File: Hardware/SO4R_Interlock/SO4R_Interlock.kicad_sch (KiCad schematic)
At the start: 143 parts, among them J1 USB-C 2.0 16P, J2 USB-C 2.0 16P, J3 USB-C 2.0 16P, J4 USB-C 2.0 16P, J5 Header 1x3, J6 RJ45_LED_Shielded, J7 8P8C_LED_Shielded_x4, Q1 2N7002, Q2 2N7002, Q3 2N7002, Q4 2N7002, Q5 2N7002, Q6 2N7002, Q7 2N7002, Q8 2N7002, U1 FT230XS, U10 TPD4E02B04DQA, U11 TPD4E02B04DQA, U12 TPD4E02B04DQA, U2 FT230XS, U3 FT230XS, U4 FT230XS, U5 74LVC1G07, U6 74LVC1G07, U7 74LVC1G07, U8 AVR32DB48x-xPT, U9 TPD4E02B04DQA

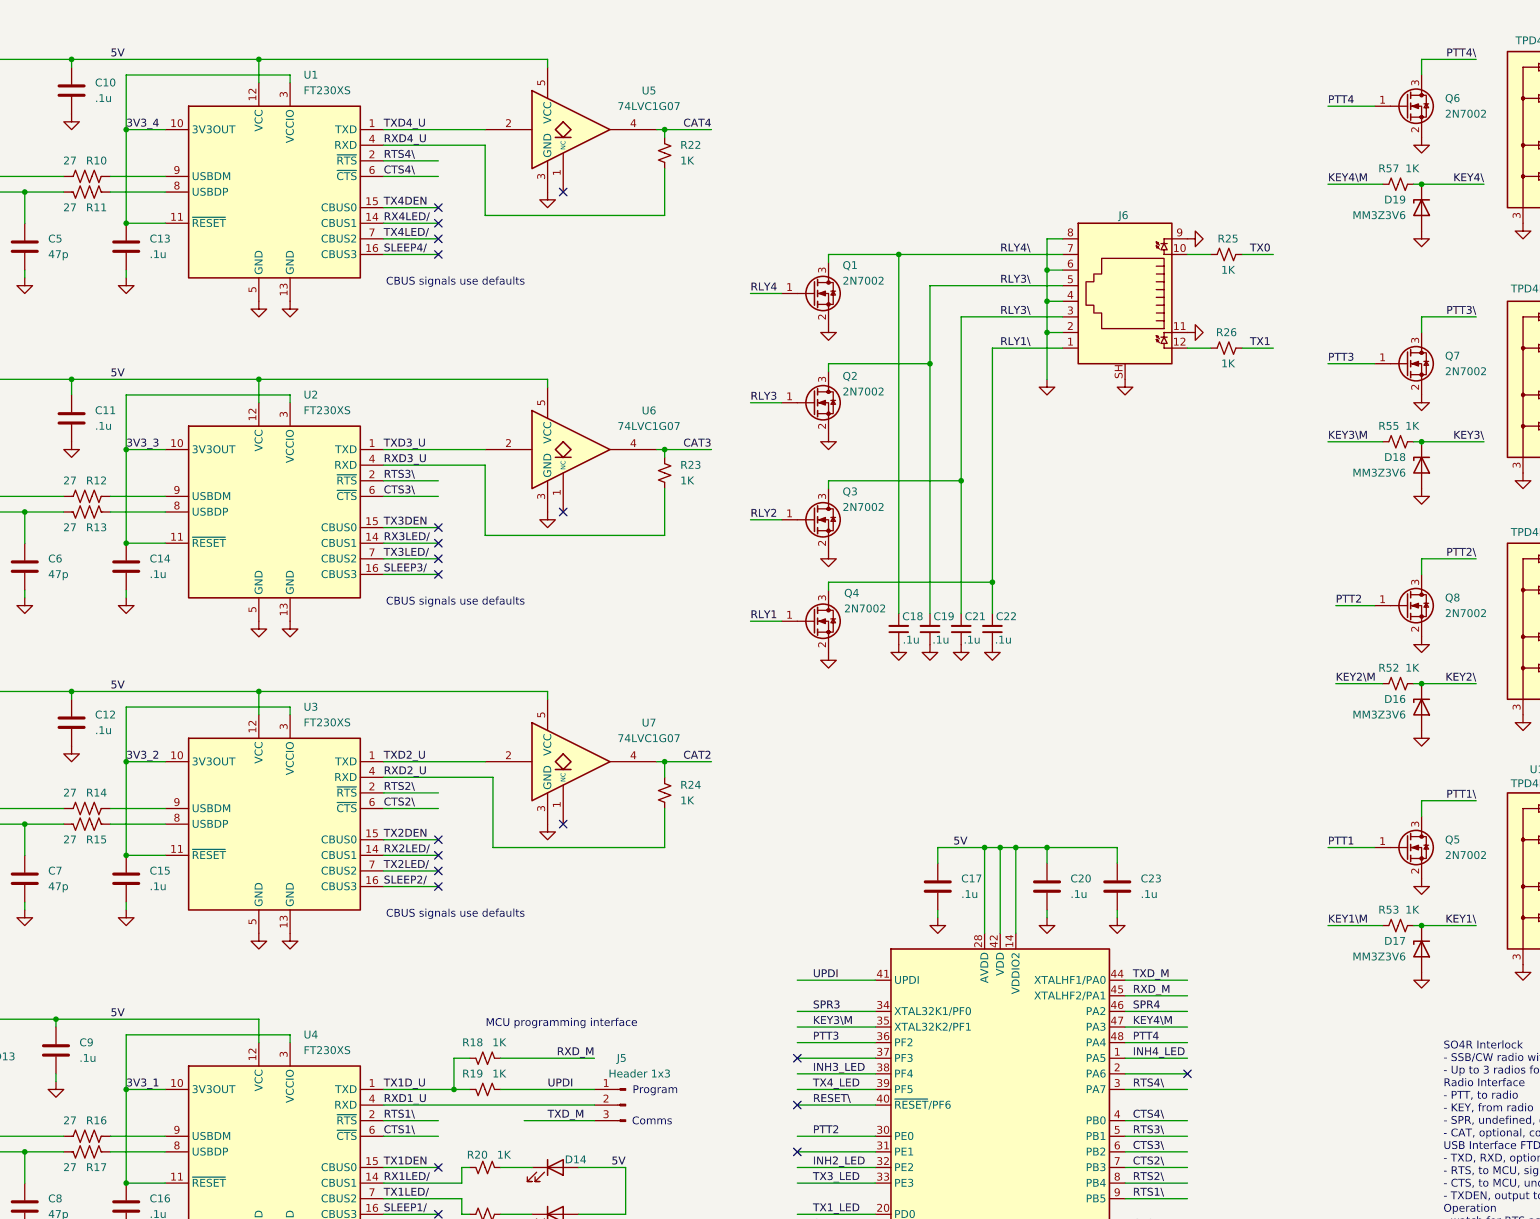
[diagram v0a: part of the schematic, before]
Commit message: Hardware   better names for PDF in documentation area   started on V2 of hardware   Connected reset\ to VDD on MCU   added .lck to .gitignore Software improves   reading RTS and KEY inputs all at one   writing KEY and PTT output as fast as possible   cleaner concept     Priority derived from RTS and KEY inputs     PTT signals derived from RTS and priority
    Relay signals derived from KEY and priority
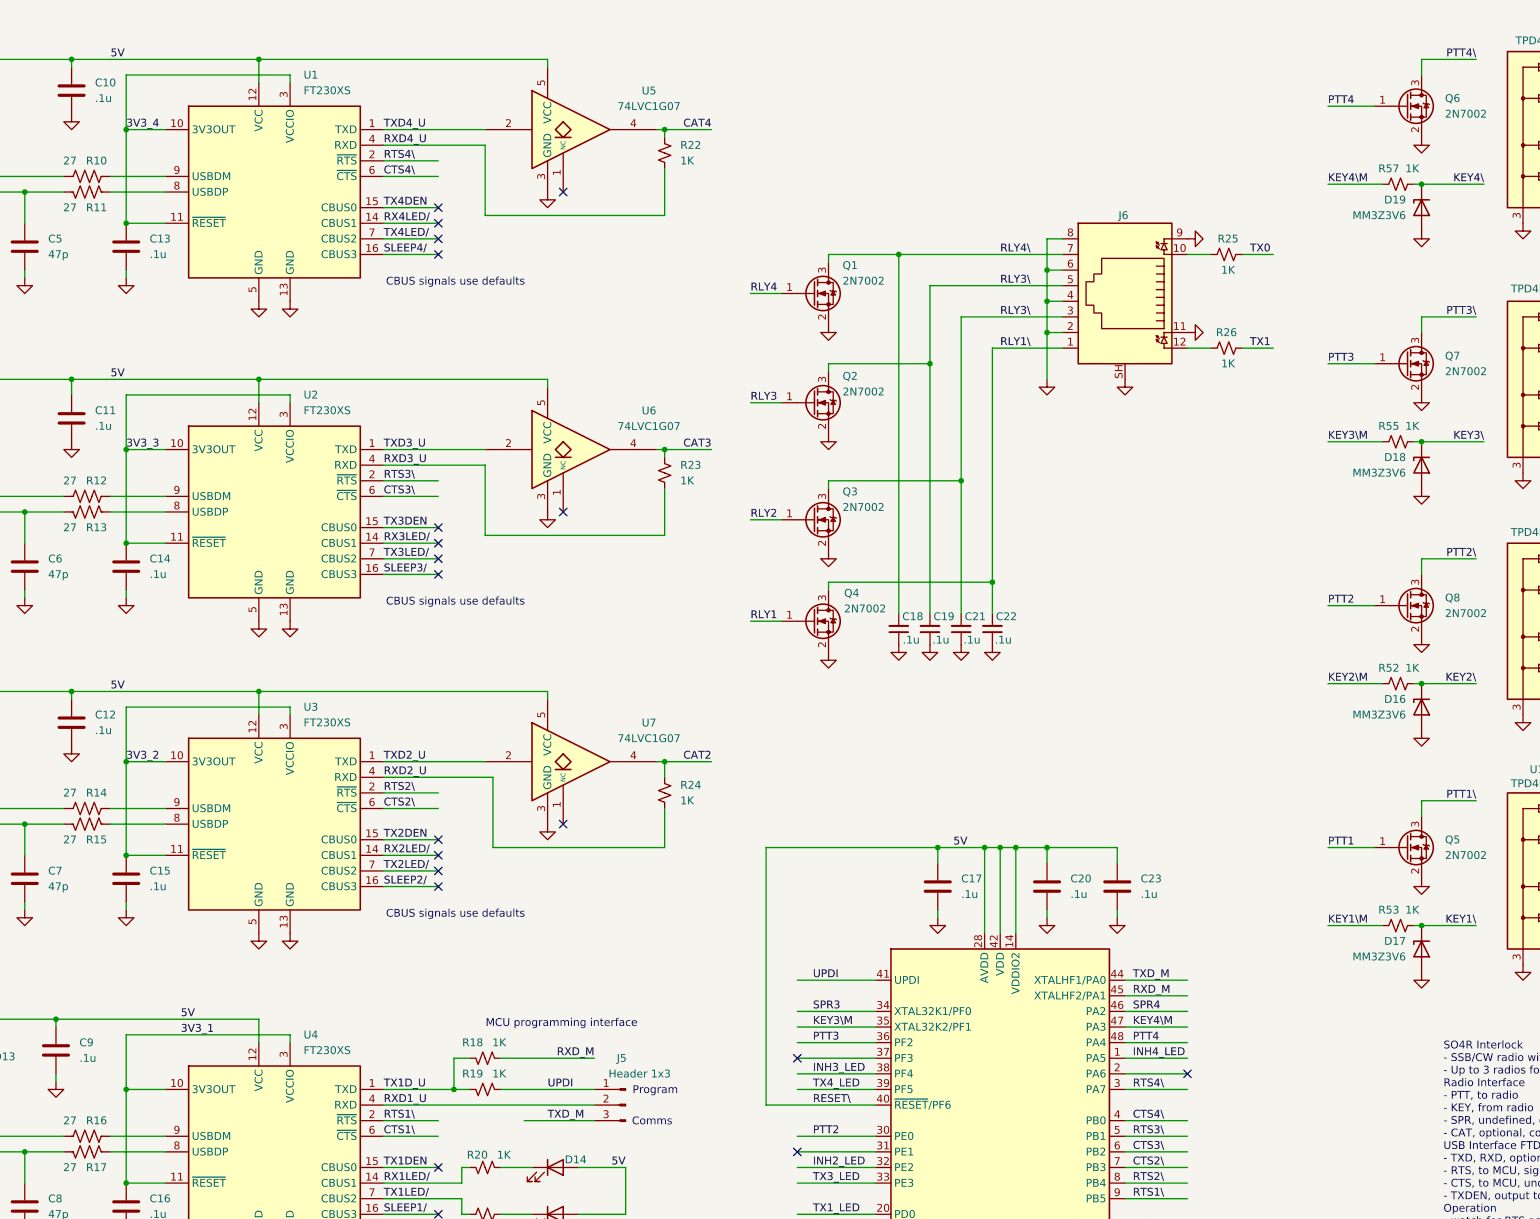
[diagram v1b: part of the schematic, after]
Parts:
- D1, D10, D11, D12, D16, D17, D18, D19, D2, D3, D4, D9: footprint Diode_SMD:D_SOD-323 -> Diode_SMD:D_SOD-523
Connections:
- net RESET\ is gone; now on net 5V: U8.40 (~{RESET}/PF6)
- no-connect marks 34 -> 33
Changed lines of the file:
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@@
 	)
 	(junction
-		(at 96.52 190.5)
-		(diameter 0)
-		(color 0 0 0 0)
-	)
-	(junction
 		(at 355.6 25.4)
 		(diameter 0)
@@
 	)
 	(junction
+		(at 96.52 190.5)
+		(diameter 0)
+		(color 0 0 0 0)
+	)
+	(junction
 		(at 45.72 96.52)
 		(diameter 0)
@@
 	)
 	(junction
+		(at 228.6 151.13)
+		(diameter 0)
+		(color 0 0 0 0)
+	)
+	(junction
 		(at 375.92 153.67)
 		(diameter 0)
@@
 	)
 	(no_connect
-		(at 205.74 193.04)
-	)
-	(no_connect
 		(at 147.32 203.2)
 	)
@@
 	(wire
 		(pts
-			(xy 96.52 190.5) (xy 102.87 190.5)
-		)
-		(stroke
-			(width 0)
-			(type default)
-		)
-	)
-	(wire
-		(pts
 			(xy 278.13 54.61) (xy 283.21 54.61)
 		)
@@
 	(wire
 		(pts
-			(xy 205.74 193.04) (xy 218.44 193.04)
-		)
-		(stroke
-			(width 0)
-			(type default)
-		)
-	)
-	(wire
-		(pts
 			(xy 123.19 128.27) (xy 123.19 129.54)
 		)
@@
 	(wire
 		(pts
+			(xy 200.66 193.04) (xy 200.66 151.13)
+		)
+		(stroke
+			(width 0)
+			(type default)
+		)
+	)
+	(wire
+		(pts
 			(xy 49.53 96.52) (xy 80.01 96.52)
 		)
@@
 	(wire
 		(pts
-			(xy 300.99 124.46) (xy 293.37 124.46)
+			(xy 300.99 124.46) (xy 292.1 124.46)
 		)
 		(stroke
@@
 	(wire
 		(pts
+			(xy 96.52 190.5) (xy 102.87 190.5)
+		)
+		(stroke
+			(width 0)
+			(type default)
+		)
+	)
+	(wire
+		(pts
 			(xy 336.55 110.49) (xy 345.44 110.49)
 		)
@@
 	(wire
 		(pts
-			(xy 293.37 111.76) (xy 299.72 111.76)
+			(xy 292.1 111.76) (xy 299.72 111.76)
 		)
 		(stroke
@@
 	(wire
 		(pts
+			(xy 200.66 193.04) (xy 218.44 193.04)
+		)
+		(stroke
+			(width 0)
+			(type default)
+		)
+	)
+	(wire
+		(pts
 			(xy 50.8 74.93) (xy 58.42 74.93)
 		)
@@
 	(wire
 		(pts
+			(xy 200.66 151.13) (xy 228.6 151.13)
+		)
+		(stroke
+			(width 0)
+			(type default)
+		)
+	)
+	(wire
+		(pts
 			(xy 63.5 58.42) (xy 63.5 53.34)
 		)
@@
 			"pb6QIMGIQA8GiT9TwmfEErfkCzE1ib5P8I/gmir5BAkSJEjwzyIhm0iQIEGC6xiJkk+QIEGC6xiJ"
 			"kk+QIEGC6xiJkk+QIEGC6xiJkk+QIEGC6xiJkk+QIEGC6xj/B2tpidjsMJ4BAAAAAElFTkSuQmCC"
+			"AAAAAAAAAAAAAAAAAAAAAAAAAAAAAAAAAAAAAAAAAAAAAAAAAAAAAAAAAAAAAAAAAAAAAAAAAAAA"
+			"AAAAAAAAAAAAAAAAAAAAAAAAAAAAAAAAAAAAAAAAAAAAAAAAAAAAAAAAAAAAAAAAAAAAAAAAAAAA"
+			"AAAAAAAAAAAAAAAAAAAAAAAAAAAAAAAAAAAAAAAAAAAAAAAAAAAAAAAAAAAAAAAAAAAAAAAAAAAA"
+			"AAAAAAAAAAAAAAAAAAAAAAAAAAAAAAAAAAAAAAAAAAAAAAAAAAAAAAAAAAAAAAAAAAAAAAAAAAAA"
+			"AAAAAAAAAAAAAAAAAAAAAAAAAAAAAAAAAAAAAAAAAAAAAAAAAAAAAAAAAAAAAAAAAAAAAAAAAAAA"
+			"AAAAAAAAAAAAAAAAAAAAAAAAAAAAAAAAAAAAAAAAAAAAAAAAAAAAAAAAAAAAAAAAAAAAAAAAAAAA"
+			"AAAAAAAAAAAAAAAAAAAAAAAAAAAAAAAAAAAAAAAAAAAAAAAAAAAAAAAAAAAAAAAAAAAAAAAAAAAA"
+			"AAAAAAAAAAAAAAAAAAAAAAAAAAAAAAAAAAAAAAAAAAAAAAAAAAAAAAAAAAAAAAAAAAAAAAAAAAAA"
+			"AAAAAAAAAAAAAAAAAAAAAAAAAAAAAAAAAAAAAAAAAAAAAAAAAAAAAAAAAAAAAAAAAAAAAAAAAAAA"
+			"AAAAAAAAAAAAAAAAAAAAAAAAAAAAAAAAAAAAAAAAAAAAAAAAAAAAAAAAAAAAAAAAAAAAAAAAAAAA"
+			"AAAAAAAAAAAAAAAAAAAAAAAAAAAAAAAAAAAAAAAAAAAAAAAAAAAAAAAAAAAAAAAAAAAAAAAAAAAA"
+			"AAAAAAAAAAAAAAAAAAAAAAAAAAAAAAAAAAAAAAAAAAAAAAAAAAAAAAAAAAAAAAAAAAAAAAAAAAAA"
+			"AAAAAAAAAAAAAAAAAAAAAAAAAAAAAAAAAAAAAAAAAAAAAAAAAAAAAAAAAAAAAAAAAAAAAAAAAAAA"
+			"AAAAAAAAAAAAAAAAAAAAAAAAAAAAAAAAAAAAAAAAAAAAAAAAAAAAAAAAAAAAAAAAAAAAAAAAAAAA"
+			"AAAAAAAAAAAAAAAAAAAAAAAAAAAAAAAAAAAAAAAAAAAAAAAAAAAAAAAAAAAAAAAAAAAAAAAAAAAA"
+			"AAAAAAAAAAAAAAAAAAAAAAAAAAAAAAAAAAAAAAAAAAAAAAAAAAAAAAAAAAAAAAAAAAAAAAAAAAAA"
+			"AAAAAAAAAAAAAAAAAAAAAAAAAAAAAAAAAAAAAAAAAAAAAAAAAAAAAAAAAAAAAAAAAAAAAAAAAAAA"
+			"AAAAAAAAAAAAAAAAAAAAAAAAAAAAAAAAAAAAAAAAAAAAAAAAAAAAAAAAAAAAAAAAAAAAAAAAAAAA"
+			"AAAAAAAAAAAAAAAAAAAAAAAAAAAAAAAAAAAAAAAAAAAAAAAAAAAAAAAAAAAAAAAAAAAAAAAAAAAA"
+			"AAAAAAAAAAAAAAAAAAAAAAAAAAAAAAAAAAAAAAAAAAAAAAAAAAAAAAAAAAAAAAAAAAAAAAAAAAAA"
+			"AAAAAAAAAAAAAAAAAAAAAAAAAAAAAAAAAAAAAAAAAAAAAAAAAAAAAAAAAAAAAAAAAAAAAAAAAAAA"
+			"AAAAAAAAAAAAAAAAAAAAAAAAAAAAAAAAAAAAAAAAAAAAAAAAAAAAAAAAAAAAAAAAAAAAAAAAAAAA"
+			"AAAAAAAAAAAAAAAAAAAAAAAAAAAAAAAAAAAAAAAAAAAAAAAAAAAAAAAAAAAAAAAAAAAAAAAAAAAA"
+			"AAAAAAAAAAAAAAAAAAAAAAAAAAAAAAAAAAAAAAAAAAAAAAAAAAAAAAAAAAAAAAAAAAAAAAAAAAAA"
+			"AAAAAAAAAAAAAAAAAAAAAAAAAAAAAAAAAAAAAAAAAAAAAAAAAAAAAAAAAAAAAAAAAAAAAAAAAAAA"
+			"AAAAAAAAAAAAAAAAAAAAAAAAAAAAAAAAAAAAAAAAAAAAAAAAAAAAAAAAAAAAAAAAAAAAAAAAAAAA"
+			"AAAAAAAAAAAAAAAAAAAAAAAAAAAAAAAAAAAAAAAAAAAAAAAAAAAAAAAAAAAAAAAAAAAAAAAAAAAA"
+			"AAAAAAAAAAAAAAAAAAAAAAAAAAAAAAAAAAAAAAAAAAAAAAAAAAAAAAAAAAAAAAAAAAAAAAAAAAAA"
+			"AAAAAAAAAAAAAAAAAAAAAAAAAAAAAAAAAAAAAAAAAAAAAAAAAAAAAAAAAAAAAAAAAAAAAAAAAAAA"
+			"AAAAAAAAAAAAAAAAAAAAAAAAAAAAAAAAAAAAAAAAAAAAAAAAAAAAAAAAAAAAAAAAAAAAAAAAAAAA"
+			"AAAAAAAAAAAAAAAAAAAAAAAAAAAAAAAAAAAAAAAAAAAAAAAAAAAAAAAAAAAAAAAAAAAAAAAAAAAA"
+			"AAAAAAAAAAAAAAAAAAAAAAAAAAAAAAAAAAAAAAAAAAAAAAAAAAAAAAAAAAAAAAAAAAAAAAAAAAAA"
+			"AAAAAAAAAAAAAAAAAAAAAAAAAAAAAAAAAAAAAAAAAAAAAAAAAAAAAAAAAAAAAAAAAAAAAAAAAAAA"
+			"AAAAAAAAAAAAAAAAAAAAAAAAAAAAAAAAAAAAAAAAAAAAAAAAAAAAAAAAAAAAAAAAAAAAAAAAAAAA"
+			"AAAAAAAAAAAAAAAAAAAAAAAAAAAAAAAAAAAAAAAAAAAAAAAAAAAAAAAAAAAAAAAAAAAAAAAAAAAA"
+			"AAAAAAAAAAAAAAAAAAAAAAAAAAAAAAAAAAAAAAAAAAAAAAAAAAAAAAAAAAAAAAAAAAAAAAAAAAAA"
+			"AAAAAAAAAAAAAAAAAAAAAAAAAAAAAAAAAAAAAAAAAAAAAAAAAAAAAAAAAAAAAAAAAAAAAAAAAAAA"
+			"AAAAAAAAAAAAAAAAAAAAAAAAAAAAAAAAAAAAAAAAAAAAAAAAAAAAAAAAAAAAAAAAAAAAAAAAAAAA"
+			"AAAAAAAAAAAAAAAAAAAAAAAAAAAAAAAAAAAAAAAAAAAAAAAAAAAAAAAAAAAAAAAAAAAAAAAAAAAA"
+			"AAAAAAAAAAAAAAAAAAAAAAAAAAAAAAAAAAAAAAAAAAAAAAAAAAAAAAAAAAAAAAAAAAAAAAAAAAAA"
+			"AAAAAAAAAAAAAAAAAAAAAAAAAAAAAAAAAAAAAAAAAAAAAAAAAAAAAAAAAAAAAAAAAAAAAAAAAAAA"
+			"AAAAAAAAAAAAAAAAAAAAAAAAAAAAAAAAAAAAAAAAAAAAAAAAAAAAAAAAAAAAAAAAAAAAAAAAAAAA"
+			"AAAAAAAAAAAAAAAAAAAAAAAAAAAAAAAAAAAAAAAAAAAAAAAAAAAAAAAAAAAAAAAAAAAAAAAAAAAA"
+			"AAAAAAAAAAAAAAAAAAAAAAAAAAAAAAAAAAAAAAAAAAAAAAAAAAAAAAAAAAAAAAAAAAAAAAAAAAAA"
+			"AAAAAAAAAAAAAAAAAAAAAAAAAAAAAAAAAAAAAAAAAAAAAAAAAAAAAAAAAAAAAAAAAAAAAAAAAAAA"
+			"AAAAAAAAAAAAAAAAAAAAAAAAAAAAAAAAAAAAAAAAAAAAAAAAAAAAAAAAAAAAAAAAAAAAAAAAAAAA"
+			"AAAAAAAAAAAAAAAAAAAAAAAAAAAAAAAAAAAAAAAAAAAAAAAAAAAAAAAAAAAAAAAAAAAAAAAAAAAA"
+			"AAAAAAAAAAAAAAAAAAAAAAAAAAAAAAAAAAAAAAAAAAAAAAAAAAAAAAAAAAAAAAAAAAAAAAAAAAAA"
+			"AAAAAAAAAAAAAAAAAAAAAAAAAAAAAAAAAAAAAAAAAAAAAAAAAAAAAAAAAAAAAAAAAAAAAAAAAAAA"
+			"AAAAAAAAAAAAAAAAAAAAAAAAAAAAAAAAAAAAAAAAAAAAAAAAAAAAAAAAAAAAAAAAAAAAAAAAAAAA"
+			"AAAAAAAAAAAAAAAAAAAAAAAAAAAAAAAAAAAAAAAAAAAAAAAAAAAAAAAAAAAAAAAAAAAAAAAAAAAA"
+			"AAAAAAAAAAAAAAAAAAAAAAAAAAAAAAAAAAAAAAAAAAAAAAAAAAAAAAAAAAAAAAAAAAAAAAAAAAAA"
+			"AAAAAAAAAAAAAAAAAAAAAAAAAAAAAAAAAAAAAAAAAAAAAAAAAAAAAAAAAAAAAAAAAAAAAAAAAAAA"
+			"AAAAAAAAAAAAAAAAAAAAAAAAAAAAAAAAAAAAAAAAAAAAAAAAAAAAAAAAAAAAAAAAAAAAAAAAAA=="
 		)
 	)
@@
 	)
 	(label "KEY2\\M"
-		(at 293.37 124.46 0)
+		(at 292.1 124.46 0)
 		(effects
 			(font
@@
 	)
 	(label "3V3_1"
-		(at 96.52 190.5 0)
+		(at 105.41 181.61 0)
 		(effects
 			(font
@@
 	)
 	(label "5V"
-		(at 93.98 179.07 0)
+		(at 105.41 179.07 0)
 		(effects
 			(font
@@
 	)
 	(label "PTT2"
-		(at 293.37 111.76 0)
+		(at 292.1 111.76 0)
 		(effects
 			(font
@@
 	)
 	(symbol
-		(lib_name "LED_1")
 		(lib_id "Device:LED")
 		(at 73.66 186.69 90)
@@
 			)
 		)
-		(property "Footprint" "Diode_SMD:D_SOD-323"
+		(property "Footprint" "Diode_SMD:D_SOD-523"
 			(at 67.945 205.74 0)
 			(effects
@@
 			)
 		)
-		(property "Footprint" "Diode_SMD:D_SOD-323"
+		(property "Footprint" "Diode_SMD:D_SOD-523"
 			(at 45.085 106.68 0)
 			(effects
@@
 			)
 		)
-		(property "Footprint" "Diode_SMD:D_SOD-323"
+		(property "Footprint" "Diode_SMD:D_SOD-523"
 			(at 311.785 46.99 0)
 			(effects
@@
 			)
 		)
-		(property "Footprint" "Diode_SMD:D_SOD-323"
+		(property "Footprint" "Diode_SMD:D_SOD-523"
 			(at 45.085 157.48 0)
 			(effects
@@
 			)
 		)
-		(property "Footprint" "Diode_SMD:D_SOD-323"
+		(property "Footprint" "Diode_SMD:D_SOD-523"
 			(at 67.945 152.4 0)
 			(effects
@@
 			)
 		)
-		(property "Footprint" "Diode_SMD:D_SOD-323"
+		(property "Footprint" "Diode_SMD:D_SOD-523"
 			(at 45.085 210.82 0)
 			(effects
@@
 			)
 		)
-		(property "Footprint" "Diode_SMD:D_SOD-323"
+		(property "Footprint" "Diode_SMD:D_SOD-523"
 			(at 45.085 54.61 0)
 			(effects
@@
 			)
 		)
-		(property "Footprint" "Diode_SMD:D_SOD-323"
+		(property "Footprint" "Diode_SMD:D_SOD-523"
 			(at 67.945 101.6 0)
 			(effects
@@
 			)
 		)
-		(property "Footprint" "Diode_SMD:D_SOD-323"
+		(property "Footprint" "Diode_SMD:D_SOD-523"
 			(at 311.785 128.27 0)
 			(effects
@@
 			)
 		)
-		(property "Footprint" "Diode_SMD:D_SOD-323"
+		(property "Footprint" "Diode_SMD:D_SOD-523"
 			(at 311.785 88.9 0)
 			(effects
@@
 			)
 		)
-		(property "Footprint" "Diode_SMD:D_SOD-323"
+		(property "Footprint" "Diode_SMD:D_SOD-523"
 			(at 311.785 167.64 0)
 			(effects
@@
 			)
 		)
-		(property "Footprint" "Diode_SMD:D_SOD-323"
+		(property "Footprint" "Diode_SMD:D_SOD-523"
 			(at 67.945 49.53 0)
 			(effects
